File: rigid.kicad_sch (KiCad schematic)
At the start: 14 parts, among them J1 47219-2001, J2 Bus_PCI_Express_Mini, U1 STM32L432KCUx

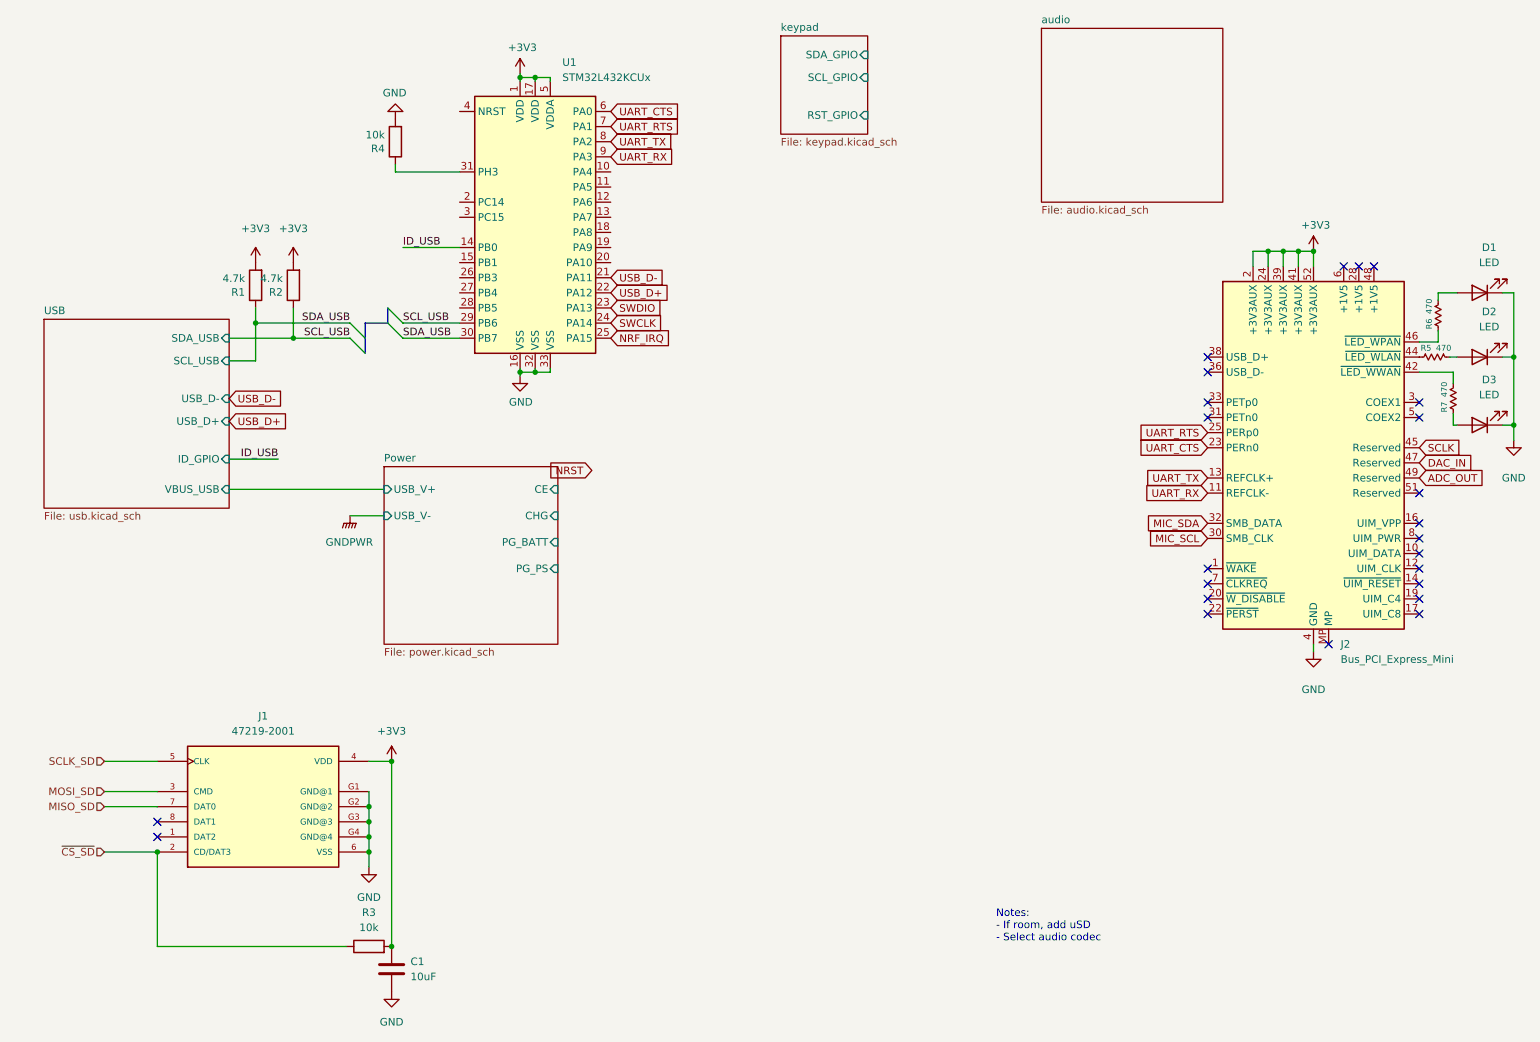
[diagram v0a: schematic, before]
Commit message: USB IC Removal
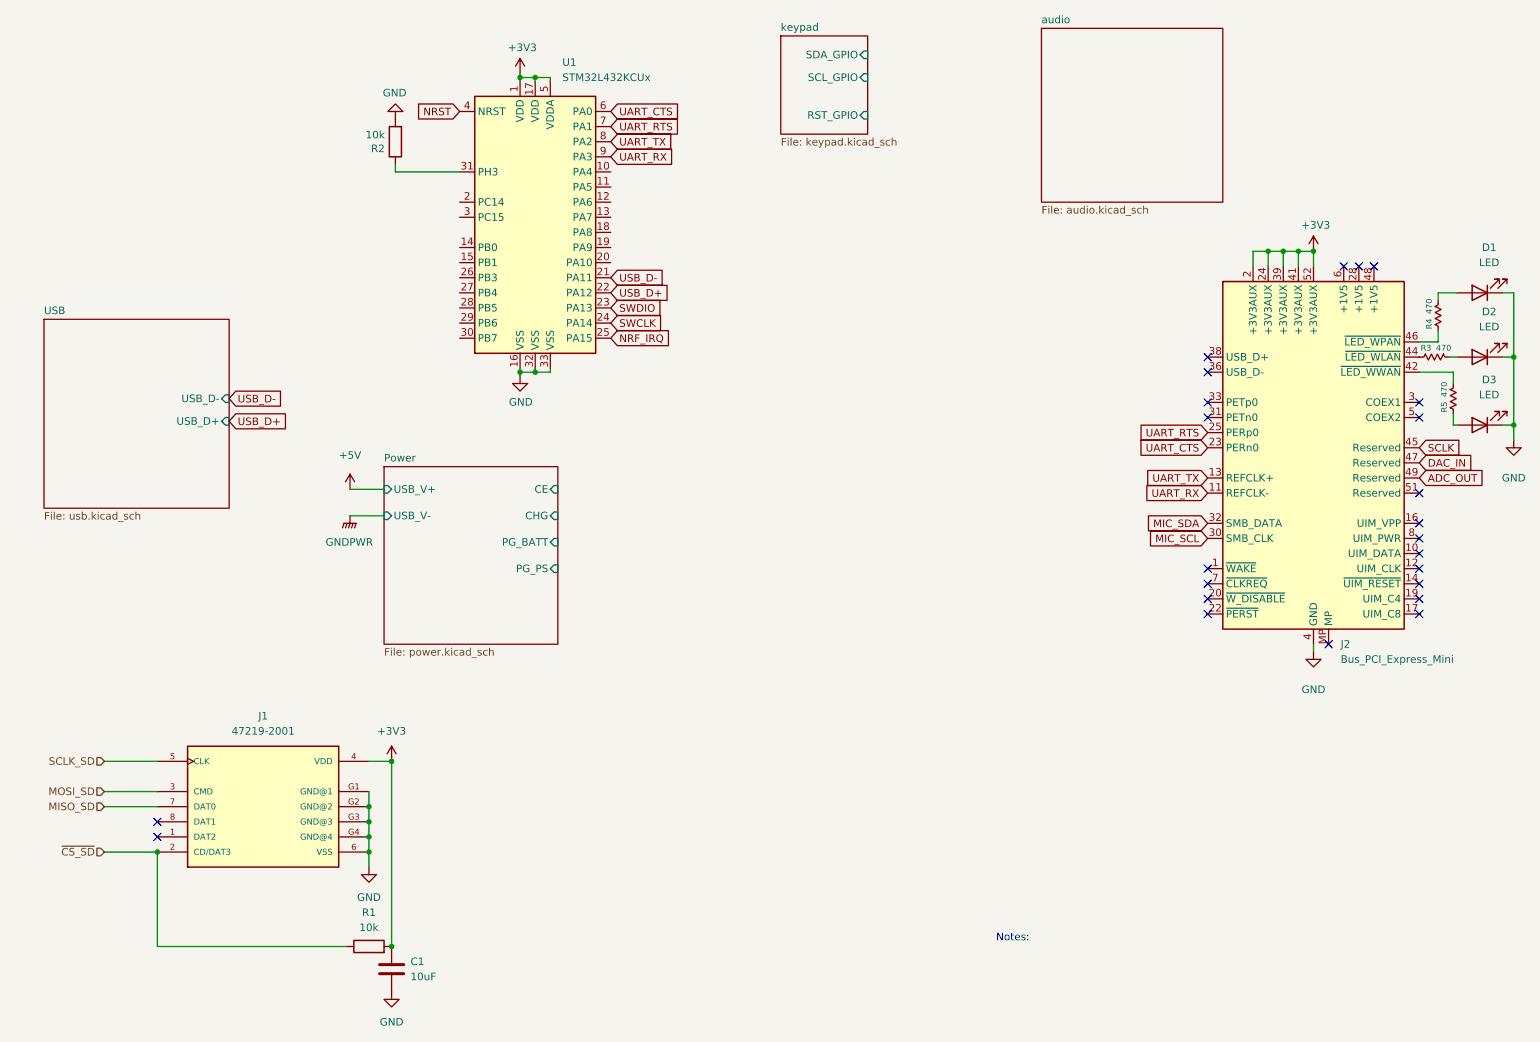
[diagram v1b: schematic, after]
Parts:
- removed R1, R2: 4.7k, Resistor_SMD:R_0402_1005Metric, symbol Device:R
- renumbered R3 to R1, R4 to R2, R5 to R3, R6 to R4, R7 to R5
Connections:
- net NRST: now also U1.4 (NRST)
- net ID_USB: no longer names the net of U1.14 (PB0)
- net SCL_USB: no longer names the net of U1.29 (PB6)
- net SDA_USB: no longer names the net of U1.30 (PB7)
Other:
- sheet USB ports: added none; removed ID_GPIO, SCL_USB, SDA_USB, VBUS_USB
- note added: "Notes:"
- note removed: "Notes: - If room, add uSD - Select audio codec"

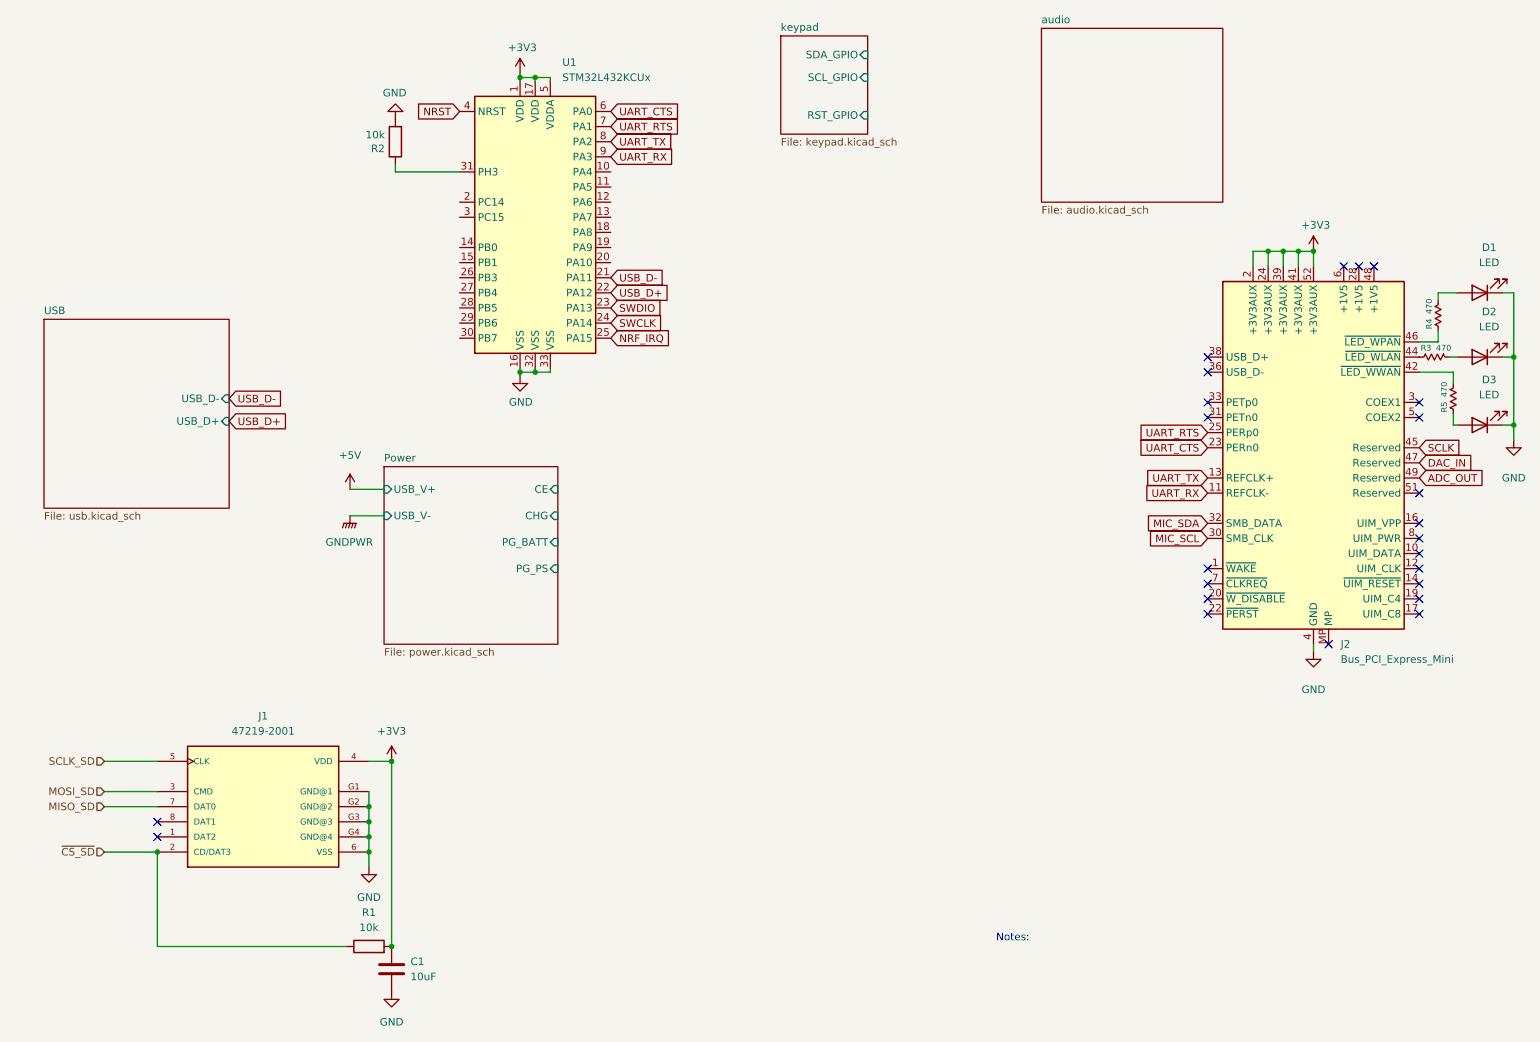
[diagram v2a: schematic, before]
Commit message: Audio near completion
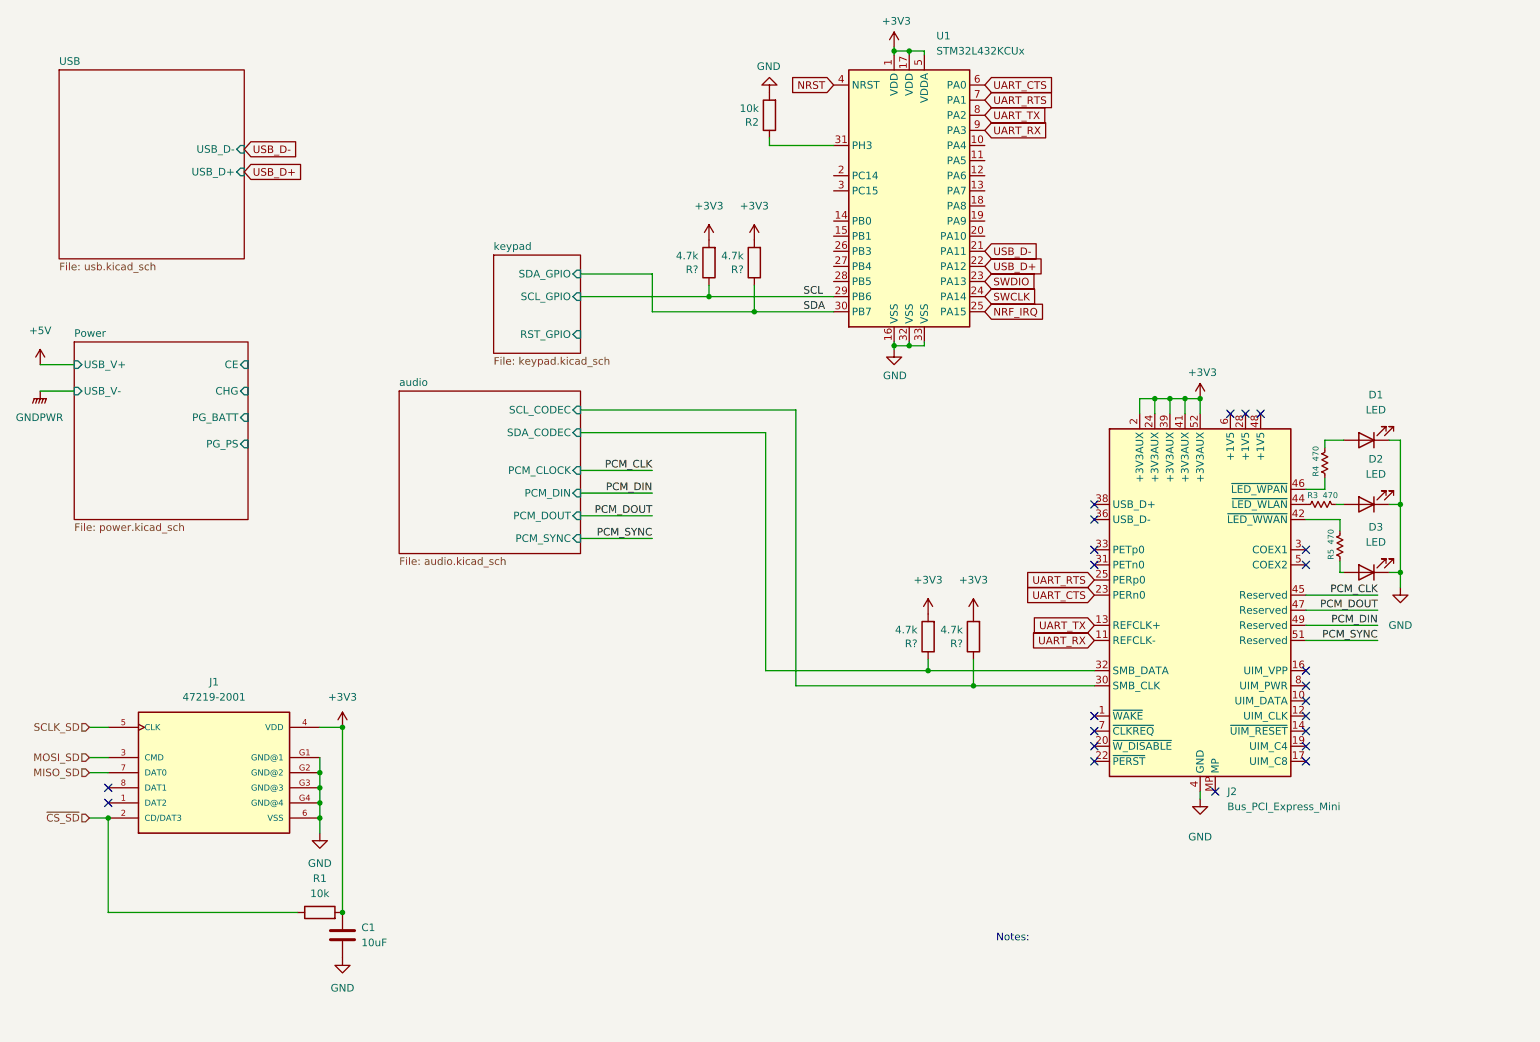
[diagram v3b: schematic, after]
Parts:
- added R? (x4): 4.7k, Resistor_SMD:R_0402_1005Metric, symbol Device:R
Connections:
- net +3V3: now also R?.2, R?.2, R?.2, R?.2
- net PCM_SYNC: now reaches J2.51 (Reserved)
- net SCL: now reaches U1.29 (PB6)
- net SCL: now also R?.1
- net SDA: now reaches U1.30 (PB7)
- net SDA: now also R?.1
- net ADC_OUT renamed PCM_DIN
- net DAC_IN renamed PCM_DOUT
- net MIC_SCL renamed audio/SCL_CODEC
- net audio/SCL_CODEC: now also R?.1
- net MIC_SDA renamed audio/SDA_CODEC
- net audio/SDA_CODEC: now also R?.1
- net SCLK renamed PCM_CLK
- no-connect marks 24 -> 23
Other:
- sheet audio ports: added PCM_CLOCK, PCM_DIN, PCM_DOUT, PCM_SYNC, SCL_CODEC, SDA_CODEC; removed none
- moved on the sheet: C1, D1, D2, D3, J1, J2, R1, R2, R3, R4, R5, U1
